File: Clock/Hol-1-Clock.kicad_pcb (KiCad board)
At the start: 2 copper layers, 109.2 x 78.7 mm, 18 parts, among them P1 CONN_2, P2 CONN_1, P3 CONN_1, SW1 SW_PUSH, U1 NE555, U2 NE555

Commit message: v1.4.4 added PCB for clock selection
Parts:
- added C6: 100nF, C1, F.Cu at (180.3, 78.7)
- added C7: 100nF, C1, F.Cu at (171.4, 67.3)
- added D2: LED, LED-5MM, F.Cu at (182.9, 88.9)
- added P4: CONN_2, PIN_ARRAY_2X1, F.Cu at (182.9, 99.1)
- added P5: CONN_2, PIN_ARRAY_2X1, F.Cu at (160.0, 111.8)
- added P6: CONN_2, PIN_ARRAY_2X1, F.Cu at (171.4, 64.8)
- added R6: 1kΩ, R4, F.Cu at (162.6, 80.0)
- added R7: 1kΩ, R4, F.Cu at (160.0, 85.1)
- added SW2: SPDT, MICROSWITCH_SPST, F.Cu at (162.6, 67.3)
- added U3: NE555, DIP-8__300, F.Cu at (171.4, 76.2)
- added U4: 74LS00, DIP-14, F.Cu at (171.4, 115.6)
- added U5: 74LS04, DIP-14, F.Cu at (171.4, 95.2)
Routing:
- net GND: track 94.0 -> 200.7 mm, vias 0 -> 2
- net +5V: track 86.4 -> 156.2 mm, vias 2 -> 4
- net N-0000011: track 0.00 -> 38.1 mm
- net N-000003: track 0.00 -> 30.5 mm
- net N-0000014: track 0.00 -> 27.9 mm
- net N-0000016: track 0.00 -> 20.3 mm
- net N-0000019: track 0.00 -> 15.2 mm
- net N-0000021: track 0.00 -> 15.2 mm
- net N-0000022: track 0.00 -> 12.7 mm
- net N-0000024: track 0.00 -> 12.7 mm
- net N-0000020: track 0.00 -> 12.7 mm
- net N-0000013: track 0.00 -> 10.2 mm
- net N-0000025: track 0.00 -> 7.62 mm
- net N-0000015: track 0.00 -> 7.62 mm
- net N-0000012: track 0.00 -> 7.62 mm
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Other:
- board text added: "CLOCK SELECT"
- board text added: "Clock Output HALT signal"
- board text added: "Clock Source A B"

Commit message: v1.4.5 don't drive an LED directly from the clock output
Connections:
- D2 pad 1: N-0000021 (its old number) -> N-0000017
- P4 pad 1: N-0000021 (its old number) -> N-0000018
- U4 pad 11: N-000003 (its old number) -> N-0000019
- U5 pad 10: N-0000021 (its old number) -> N-0000018
- U5 pad 11: N-000003 (its old number) -> N-0000019
- U5 pad 12: (no net) -> N-0000017
- U5 pad 13: (no net) -> N-0000019
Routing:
- net N-0000019: track 0.00 -> 40.6 mm
- net N-000003 (its old number): track 30.5 -> 0.00 mm
- net N-0000021 (its old number): track 15.2 -> 0.00 mm
- net N-0000017: track 0.00 -> 10.2 mm
- net N-0000018: track 0.00 -> 7.62 mm

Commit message: v1.5.0 Memory Management Unit (MMU) schematic first draft
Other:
- board text added: "Incorporates two circuits originally designed for 10x24 via boards."
- board text removed: "Incorporates two circuits originally designed for a 10x24 via boards."
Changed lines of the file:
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@@
     (effects (font (size 1.5 1.5) (thickness 0.3)))
   )
-  (gr_text "Incorporates two circuits originally designed for a 10x24 via boards." (at 147.32 129.54) (layer Dwgs.User)
+  (gr_text "Incorporates two circuits originally designed for 10x24 via boards." (at 147.32 129.54) (layer Dwgs.User)
     (effects (font (size 1.5 1.5) (thickness 0.3)))
   )
@@
   (segment (start 160.02 80.01) (end 167.64 80.01) (width 0.254) (layer B.Cu) (net 7))
   (segment (start 167.64 110.49) (end 160.02 110.49) (width 0.254) (layer F.Cu) (net 8))
-  (segment (start 175.26 92.71) (end 182.88 92.71) (width 0.254) (layer B.Cu) (net 9) (status 400000))
-  (segment (start 182.88 92.71) (end 182.88 90.17) (width 0.254) (layer B.Cu) (net 9) (status 800000))
+  (segment (start 175.26 92.71) (end 182.88 92.71) (width 0.254) (layer B.Cu) (net 9))
+  (segment (start 182.88 92.71) (end 182.88 90.17) (width 0.254) (layer B.Cu) (net 9))
   (segment (start 182.88 97.79) (end 175.26 97.79) (width 0.254) (layer B.Cu) (net 10))
-  (segment (start 175.26 90.17) (end 180.34 90.17) (width 0.254) (layer F.Cu) (net 11) (status 400000))
+  (segment (start 175.26 90.17) (end 180.34 90.17) (width 0.254) (layer F.Cu) (net 11))
   (segment (start 180.34 90.17) (end 180.34 95.25) (width 0.254) (layer F.Cu) (net 11))
   (segment (start 175.26 95.25) (end 180.34 95.25) (width 0.254) (layer F.Cu) (net 11))

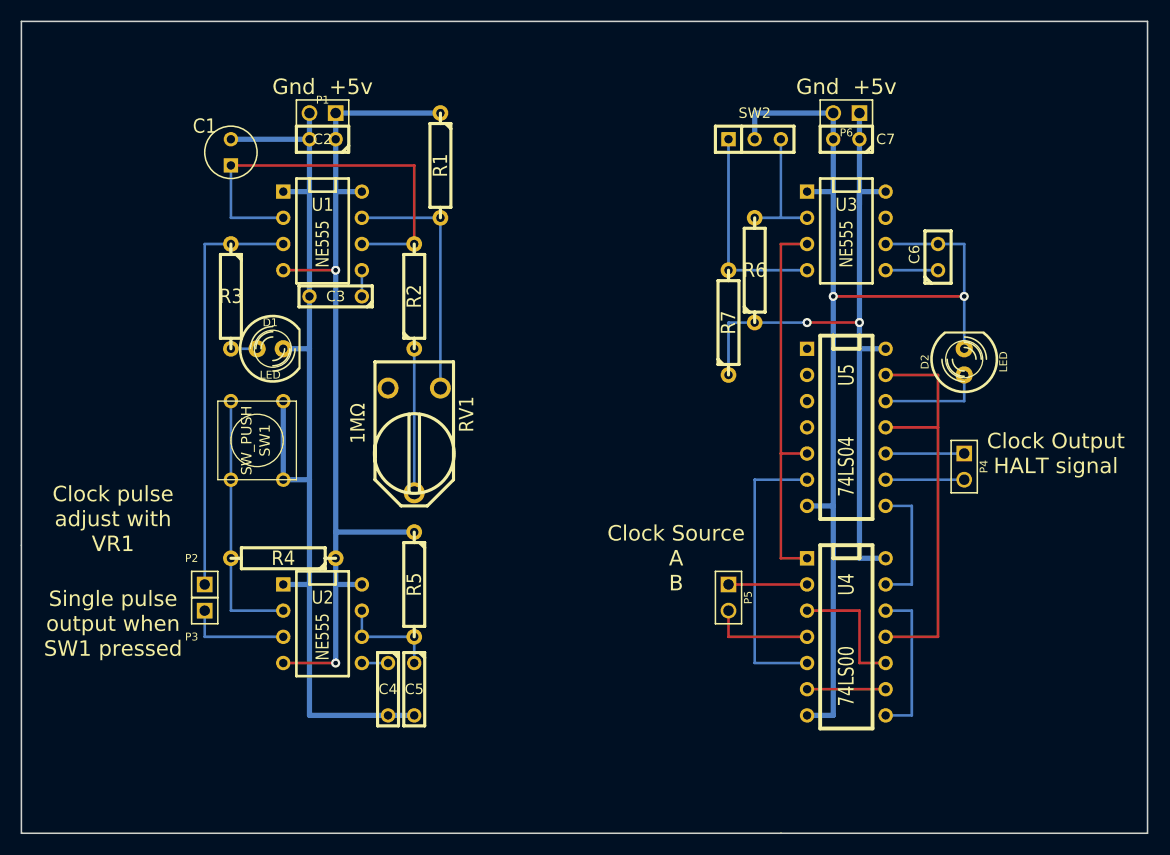
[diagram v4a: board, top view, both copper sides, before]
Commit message: 1.5.21 upgraded to KiCad 6.0
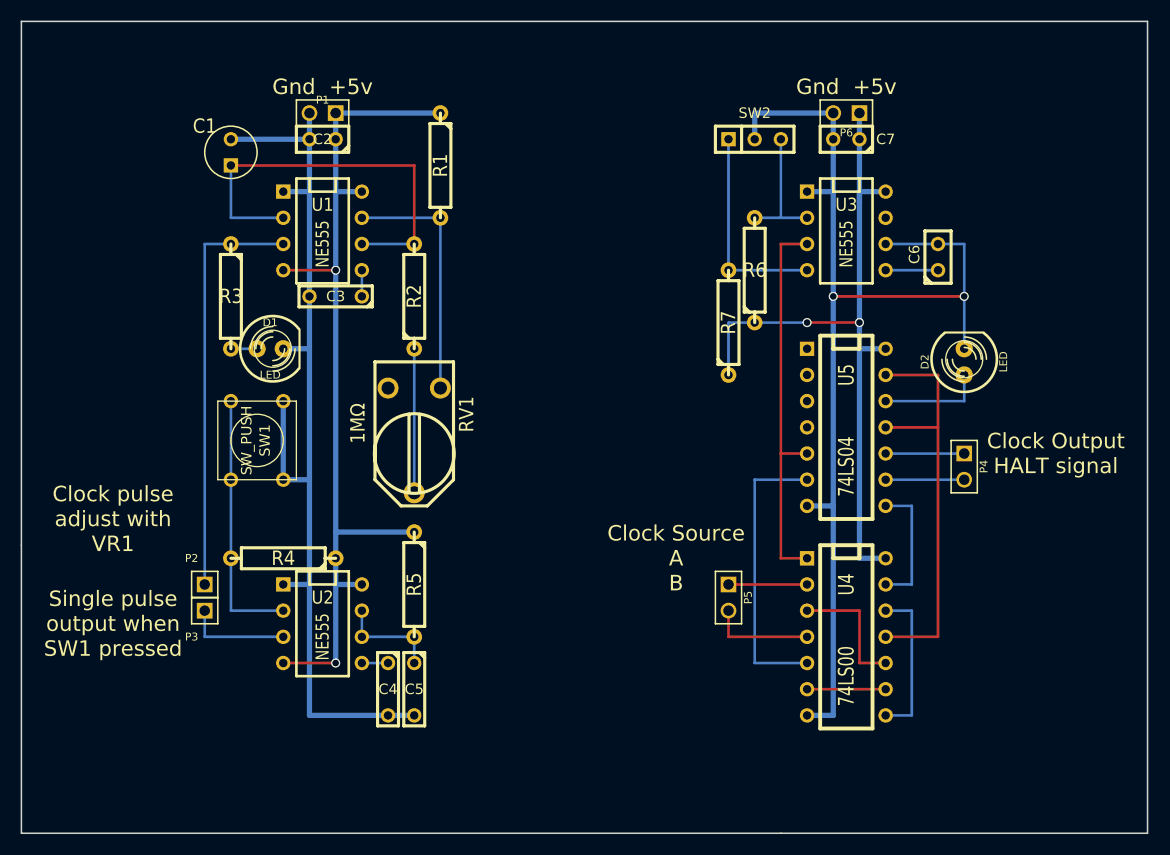
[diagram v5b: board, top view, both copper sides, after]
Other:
- net class Default removed
